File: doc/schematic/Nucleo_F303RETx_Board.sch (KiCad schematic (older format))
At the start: 37 parts, among them CN1 CONN_01X10, CN2 CONN_01X08, CN3 CONN_02X19, CN4 CONN_02X19, CN5 CONN_01X08, CN6 CONN_01X06, J4 Ina_Sensor, J5 Fan, J6 SerialDebug, J7 LCD_Board, J8 Programing, J9 Remote, P11 Rotary Encoder Board, P12 Power Board, P13 Basis, P5 TempSens, Q10 BD135, Q8 BD135, Q9 BD135, U3 93CxxA, U4 CA3140

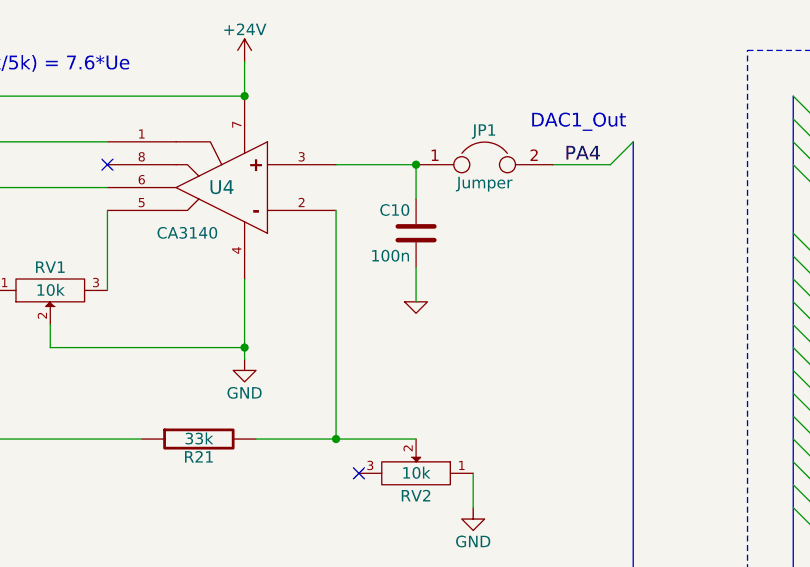
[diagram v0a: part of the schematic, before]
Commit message: Umstellung auf ST CubeIDE
Signed-off-by: Linoprit <haraldgraef@web.de>
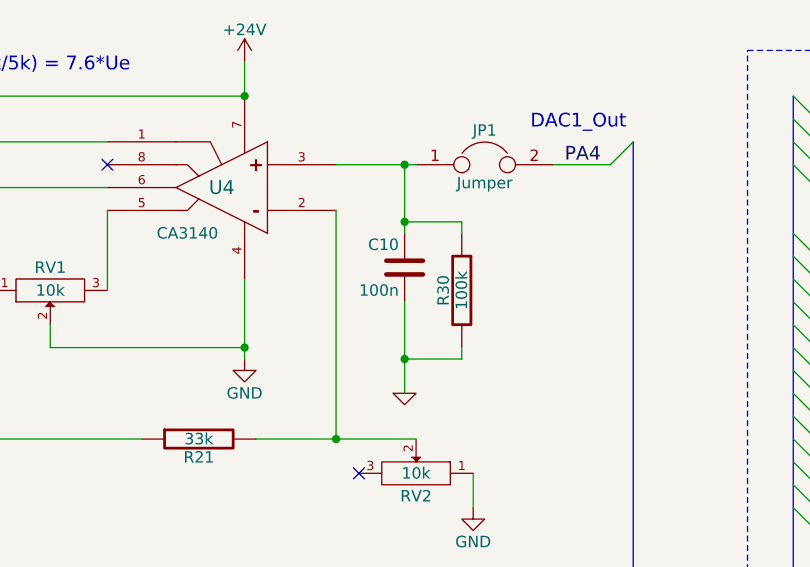
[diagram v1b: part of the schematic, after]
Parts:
- added R30: 100k, symbol Netzteil_Progammable-rescue:R-RESCUE-Netzteil_Progammable
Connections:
- net GND: now also R30.2
- net at C10.1, JP1.1, U4.3 (NON): now also R30.1
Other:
- moved on the sheet: C10
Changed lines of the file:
@@
 L Netzteil_Progammable-rescue:C C10
 U 1 1 589BF67E
-P 4700 1700
-F 0 "C10" H 4725 1800 50  0000 L CNN
-F 1 "100n" H 4725 1600 50  0000 L CNN
-F 2 "" H 4738 1550 50  0001 C CNN
-F 3 "" H 4700 1700 50  0000 C CNN
-	1    4700 1700
+P 4650 1850
+F 0 "C10" H 4675 1950 50  0000 L CNN
+F 1 "100n" H 4675 1750 50  0000 L CNN
+F 2 "" H 4688 1700 50  0001 C CNN
+F 3 "" H 4650 1850 50  0000 C CNN
+	1    4650 1850
 	-1   0    0    -1
 $EndComp
@@
 L Netzteil_Progammable-rescue:GND-RESCUE-Netzteil_Progammable #PWR041
 U 1 1 589BF775
-P 4700 2000
-F 0 "#PWR041" H 4700 2000 30  0001 C CNN
-F 1 "GND" H 4700 1930 30  0001 C CNN
-F 2 "" H 4700 2000 60  0001 C CNN
-F 3 "" H 4700 2000 60  0001 C CNN
-	1    4700 2000
-	1    0    0    -1
-$EndComp
-Wire Wire Line
-	4700 1550 4700 1400
-Wire Wire Line
-	4700 1850 4700 2000
+P 4650 2400
+F 0 "#PWR041" H 4650 2400 30  0001 C CNN
+F 1 "GND" H 4650 2330 30  0001 C CNN
+F 2 "" H 4650 2400 60  0001 C CNN
+F 3 "" H 4650 2400 60  0001 C CNN
+	1    4650 2400
+	1    0    0    -1
+$EndComp
+Wire Wire Line
+	4650 2000 4650 2250
 $Comp
 L Netzteil_Progammable-rescue:C C11
@@
 	5300 1400 5550 1400
 Wire Wire Line
-	4700 1400 4350 1400
-Connection ~ 4700 1400
+	4700 1400 4650 1400
 $Comp
 L Netzteil_Progammable-rescue:R-RESCUE-Netzteil_Progammable R25
@@
 Wire Wire Line
 	4950 4150 5250 4150
+$Comp
+L Netzteil_Progammable-rescue:R-RESCUE-Netzteil_Progammable R30
+U 1 1 5EEAE75B
+P 4900 1950
+F 0 "R30" V 4980 1950 50  0000 C CNN
+F 1 "100k" V 4900 1950 50  0000 C CNN
+F 2 "" H 4900 1950 60  0001 C CNN
+F 3 "" H 4900 1950 60  0001 C CNN
+	1    4900 1950
+	-1   0    0    -1
+$EndComp
+Wire Wire Line
+	4650 1700 4650 1650
+Wire Wire Line
+	4650 1650 4900 1650
+Wire Wire Line
+	4900 1650 4900 1700
+Wire Wire Line
+	4650 1650 4650 1400
+Connection ~ 4650 1650
+Connection ~ 4650 1400
+Wire Wire Line
+	4650 1400 4350 1400
+Wire Wire Line
+	4900 2200 4900 2250
+Wire Wire Line
+	4900 2250 4650 2250
+Connection ~ 4650 2250
+Wire Wire Line
+	4650 2250 4650 2400
 Wire Bus Line
 	4550 3500 10650 3500
